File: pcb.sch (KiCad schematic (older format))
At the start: 39 parts, among them J1 230VAC IN, J10 DHT22 2, J11 DHT22 3, J12 LIGHTS, J2 12VDC IN, J3 40HAT, J4 CONN_01X02, J5 CONN_02X02, J6 FAN 1, J7 FAN 2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

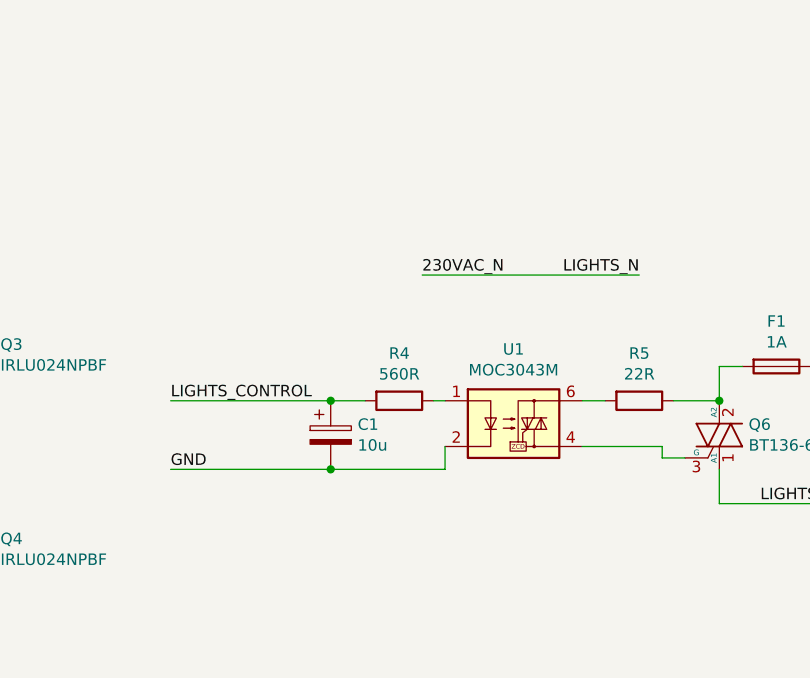
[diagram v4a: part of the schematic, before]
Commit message: Connect devices 3.3V to HAT's 3.3V
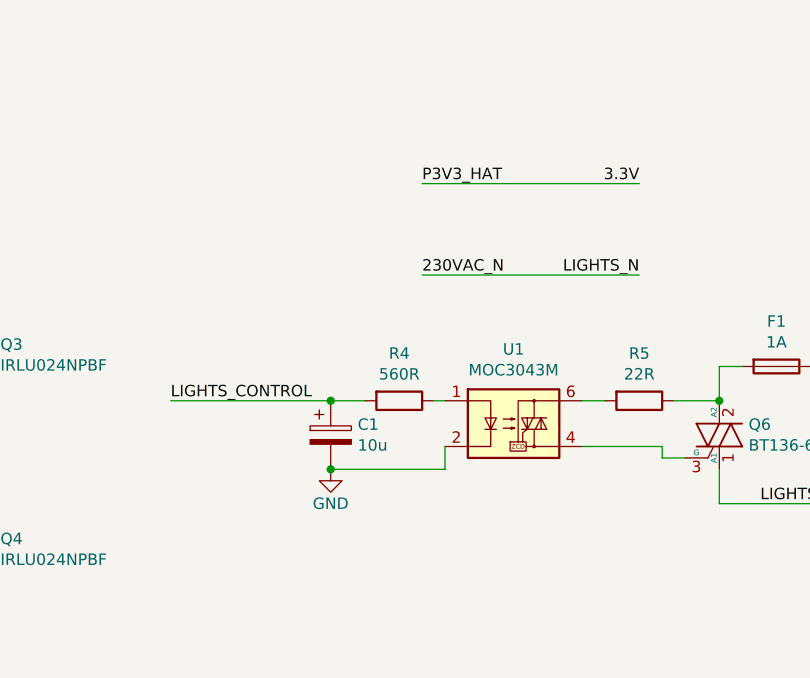
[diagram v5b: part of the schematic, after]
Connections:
- net P3V3_HAT is gone; now on net 3.3V: J3.1 (P3V3), J5.2 (Pin_2), R7.1
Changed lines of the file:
@@
 Text Label 4400 3250 2    50   ~ 0
 FAN_3_CONTROL
-Text Label 11600 6750 0    50   ~ 0
-GND
 Text Label 11600 6450 0    50   ~ 0
 LIGHTS_CONTROL
 Wire Wire Line
 	11600 6450 12300 6450
-Wire Wire Line
-	11600 6750 12300 6750
 Text Label 800  2950 0    50   ~ 0
 LIGHTS_CONTROL
+Wire Wire Line
+	12700 5500 13650 5500
+Text Label 12700 5500 0    50   ~ 0
+P3V3_HAT
+Text Label 13650 5500 2    50   ~ 0
+3.3V
+$Comp
+L power:GND #PWR?
+U 1 1 5FD8CF0B
+P 12300 6750
+F 0 "#PWR?" H 12300 6500 50  0001 C CNN
+F 1 "GND" H 12300 6600 50  0000 C CNN
+F 2 "" H 12300 6750 50  0000 C CNN
+F 3 "" H 12300 6750 50  0000 C CNN
+	1    12300 6750
+	1    0    0    -1
+$EndComp
 $EndSCHEMATC
